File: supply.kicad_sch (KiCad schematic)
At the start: 55 parts, among them Q1 BSS138PW,115, U21 TPS62A06DRLR, U302 AP62301_TSOT, U40 SIC431AED-T1-GE3

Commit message: [#100765] Update schematic
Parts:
- removed C306, C314, C317: C_22u_25V_0805, antmicro-footprints:C_0805_2012Metric, symbol antmicroCapacitorsmisc:C_22u_25V_0805
- removed C309: C_100n_0402, antmicro-footprints:C_0402_1005Metric, symbol antmicroCapacitors0402:C_100n_0402
- removed C88, C89, C90, C91: C_10u_0402, antmicro-footprints:C_0402_1005Metric, symbol antmicroCapacitors0402:C_10u_0402
- removed L3: L_2u2_5.8A_WE-PMFI-35329222, antmicro-footprints:L_WE-PMFI-353220, symbol antmicroFixedInductors:L_2u2_5.8A_WE-PMFI-35329222
- removed R179: R_0R_22.4A_0603, jetson-orin-baseboard-footprints:R_0603_1608Metric, symbol jetson-orin-baseboard:R_0R_22.4A_0603
- removed R18: R_12k4_0402, antmicro-footprints:R_0402_1005Metric, symbol antmicroResistors0402:R_12k4_0402
- removed R19: R_13k7_0402, antmicro-footprints:R_0402_1005Metric, symbol antmicroResistors0402:R_13k7_0402
- removed R20: R_47k_0402, antmicro-footprints:R_0402_1005Metric, symbol antmicroResistors0402:R_47k_0402
- removed R312: R_10k_0402, antmicro-footprints:R_0402_1005Metric, symbol antmicroResistors0402:R_10k_0402
- removed R323: R_0R_22.4A_0603, antmicro-footprints:R_0603_1608Metric, symbol antmicroResistors0603:R_0R_22.4A_0603
- removed TP309: TP_0.75mm_SMD, antmicro-footprints:TP_SMD_0.75mm, symbol antmicroTestPoints:TP_0.75mm_SMD
- removed U302: AP62301_TSOT, antmicro-footprints:TSOT23-6, symbol antmicroDCDCConverters:AP62301_TSOT
- added C60, C61: C_47u_0603, antmicro-footprints:C_0603_1608Metric, symbol antmicroCapacitors0603:C_47u_0603
- added C62, C63: C_22u_0603, antmicro-footprints:C_0603_1608Metric, symbol antmicroCapacitors0603:C_22u_0603
- added C84, C85: C_10u_0402, antmicro-footprints:C_0402_1005Metric, symbol antmicroCapacitors0402:C_10u_0402
- added C86: C_1u_0402, antmicro-footprints:C_0402_1005Metric, symbol antmicroCapacitors0402:C_1u_0402
- added C92: C_120p_100V_0402, antmicro-footprints:C_0402_1005Metric, symbol antmicroCapacitors0402:C_120p_100V_0402
- added D18: LED_G_0603_LG_L29K-G2J1-24-Z, antmicro-footprints:LED_0603_1608Metric_G, symbol antmicroLEDIndicationDiscrete:LED_G_0603_LG_L29K-G2J1-24-Z
- added L4: L_220n_5.9A_1008, antmicro-footprints:L_1008_2520Metric, symbol antmicroFixedInductors:L_220n_5.9A_1008
- added Q6: BSS138PW,115, antmicro-footprints:SC70-3, symbol antmicroTransistorsFETsMOSFETsSingle:BSS138PW,115
- added R148: R_100k_0.1%_0402, antmicro-footprints:R_0402_1005Metric, symbol antmicroResistors0402:R_100k_0402
- added R20: R_470R_0402, antmicro-footprints:R_0402_1005Metric, symbol antmicroResistors0402:R_470R_0402
- added R69, R81: R_0R_22.4A_0603, antmicro-footprints:R_0603_1608Metric, symbol antmicroResistors0603:R_0R_22.4A_0603
- added R77: R_1k5_0402, antmicro-footprints:R_0402_1005Metric, symbol antmicroResistors0402:R_1k5_0402
- added R78: R_10k_0402, antmicro-footprints:R_0402_1005Metric, symbol antmicroResistors0402:R_10k_0402
- added R79: R_33R_0402, antmicro-footprints:R_0402_1005Metric, symbol antmicroResistors0402:R_33R_0402
- added R80: R_200k_0402, antmicro-footprints:R_0402_1005Metric, symbol antmicroResistors0402:R_200k_0402
- added TP30: TP_1mm_SMD, antmicro-footprints:TP_SMD_1mm, symbol antmicroTestPoints:TP_1mm_SMD
- added U22: TPS62A06DRLR, antmicro-footprints:SOT-563, symbol antmicroDCDCConverters:TPS62A06DRLR
- C121, C125: footprint jetson-orin-baseboard-footprints:C_0402_1005Metric -> antmicro-footprints:C_0402_1005Metric; symbol jetson-orin-baseboard:C_100n_0402 -> antmicroCapacitors0402:C_100n_0402
- C122, C151: footprint jetson-orin-baseboard-footprints:C_0805_2012Metric -> antmicro-footprints:C_0805_2012Metric; symbol jetson-orin-baseboard:C_22u_25V_0805 -> antmicroCapacitorsmisc:C_22u_25V_0805
- C123: footprint jetson-orin-baseboard-footprints:C_0402_1005Metric -> antmicro-footprints:C_0402_1005Metric; symbol jetson-orin-baseboard:C_1u_0402 -> antmicroCapacitors0402:C_1u_0402
- C126, C127, C128, C154: footprint jetson-orin-baseboard-footprints:C_0603_1608Metric_EIA -> antmicro-footprints:C_0603_1608Metric_EIA; symbol jetson-orin-baseboard:C_22u_16V_0603 -> antmicroCapacitors0603:C_22u_16V_0603
- C155: footprint jetson-orin-baseboard-footprints:C_0402_1005Metric -> antmicro-footprints:C_0402_1005Metric; symbol jetson-orin-baseboard:C_4u7_25V_0402 -> antmicroCapacitors0402:C_4u7_25V_0402
- D33: footprint jetson-orin-baseboard-footprints:SOD-923 -> antmicro-footprints:SOD-923; symbol jetson-orin-baseboard:ESD9X5.0ST5G -> antmicroTVSDiodes:ESD9X5.0ST5G
- L1: footprint jetson-orin-baseboard-footprints:L_Bourns-SRP5030CA -> antmicro-footprints:L_Bourns-SRP5030CA; symbol jetson-orin-baseboard:L_560n_17.7A_Bourns-SRP5030CA -> antmicroFixedInductors:L_560n_17.7A_Bourns-SRP5030CA
- R147: symbol antmicroResistors0402:R_100k_0.1%_0402 -> antmicroResistors0402:R_100k_0402; MPN RC0402BR-07100KL -> CR0402-FX-1003GLF; Manufacturer YAGEO -> Bourns; Tolerance 0.1% -> 1%
- R173, R176: footprint jetson-orin-baseboard-footprints:R_0402_1005Metric -> antmicro-footprints:R_0402_1005Metric; symbol jetson-orin-baseboard:R_499k_0402 -> antmicroResistors0402:R_499k_0402
- R178: footprint jetson-orin-baseboard-footprints:R_0603_1608Metric -> antmicro-footprints:R_0603_1608Metric; symbol jetson-orin-baseboard:R_0R_22.4A_0603 -> antmicroResistors0603:R_0R_22.4A_0603
- R240: footprint jetson-orin-baseboard-footprints:R_0402_1005Metric -> antmicro-footprints:R_0402_1005Metric; symbol jetson-orin-baseboard:R_499k_0402 -> antmicroResistors0402:R_499k_0402; now in the parts list
- TP54: footprint jetson-orin-baseboard-footprints:TP_SMD_0.75mm -> antmicro-footprints:TP_SMD_0.75mm; symbol jetson-orin-baseboard:TP_0.75mm_SMD -> antmicroTestPoints:TP_0.75mm_SMD
- U40: footprint jetson-orin-baseboard-footprints:MLP44-24L_4x4x0.75mm -> antmicro-footprints:MLP44-24L_4x4x0.75mm; symbol jetson-orin-baseboard:SIC431AED-T1-GE3 -> antmicroDCDCConverters:SIC431AED-T1-GE3
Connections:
- net +0V95: now also R69.2
- net +1V8: now also R81.2, TP30.1
- net +3V3: now also C84.2, C85.2, R20.2, R77.1, R78.2, U22.3 (VIN)
- net DCDC_EN: now also C86.1, R77.2, U22.4 (EN)
- net GND: now also C60.1, C61.1, C62.1, C63.1, C84.1, C85.1, C86.2, Q6.2 (S), R148.1, U22.1 (GND)
- net at C87.2, L2.2, R17.2: now also C60.2, C61.2, R69.1
- new net: D18.2 (A), R20.1
- new net: C62.2, C63.2, C92.2, L4.2, R80.2, R81.1
- new net: C92.1, R148.2, R80.1, U22.5 (FB)
- new net: Q6.1 (G), R78.1, R79.1
- new net: D18.1 (C), Q6.3 (D)
- new net: R79.2, U22.6 (PG)
- new net: L4.1, U22.2 (SW)
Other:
- note added: "JOB VCC to 3V3 DCDC Converter"
- note added: "PG: OD in Power Good state"
- note added: "V_{OUT} = 0.6*(200k/100k + 1)"
- note added: "V_{OUT} = 1.8V"
- note removed: "3V3 DCDC"
- moved on the sheet: C81, C82, C83, C87, D17, L2, Q1, R147, R15, R16, R17, R66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

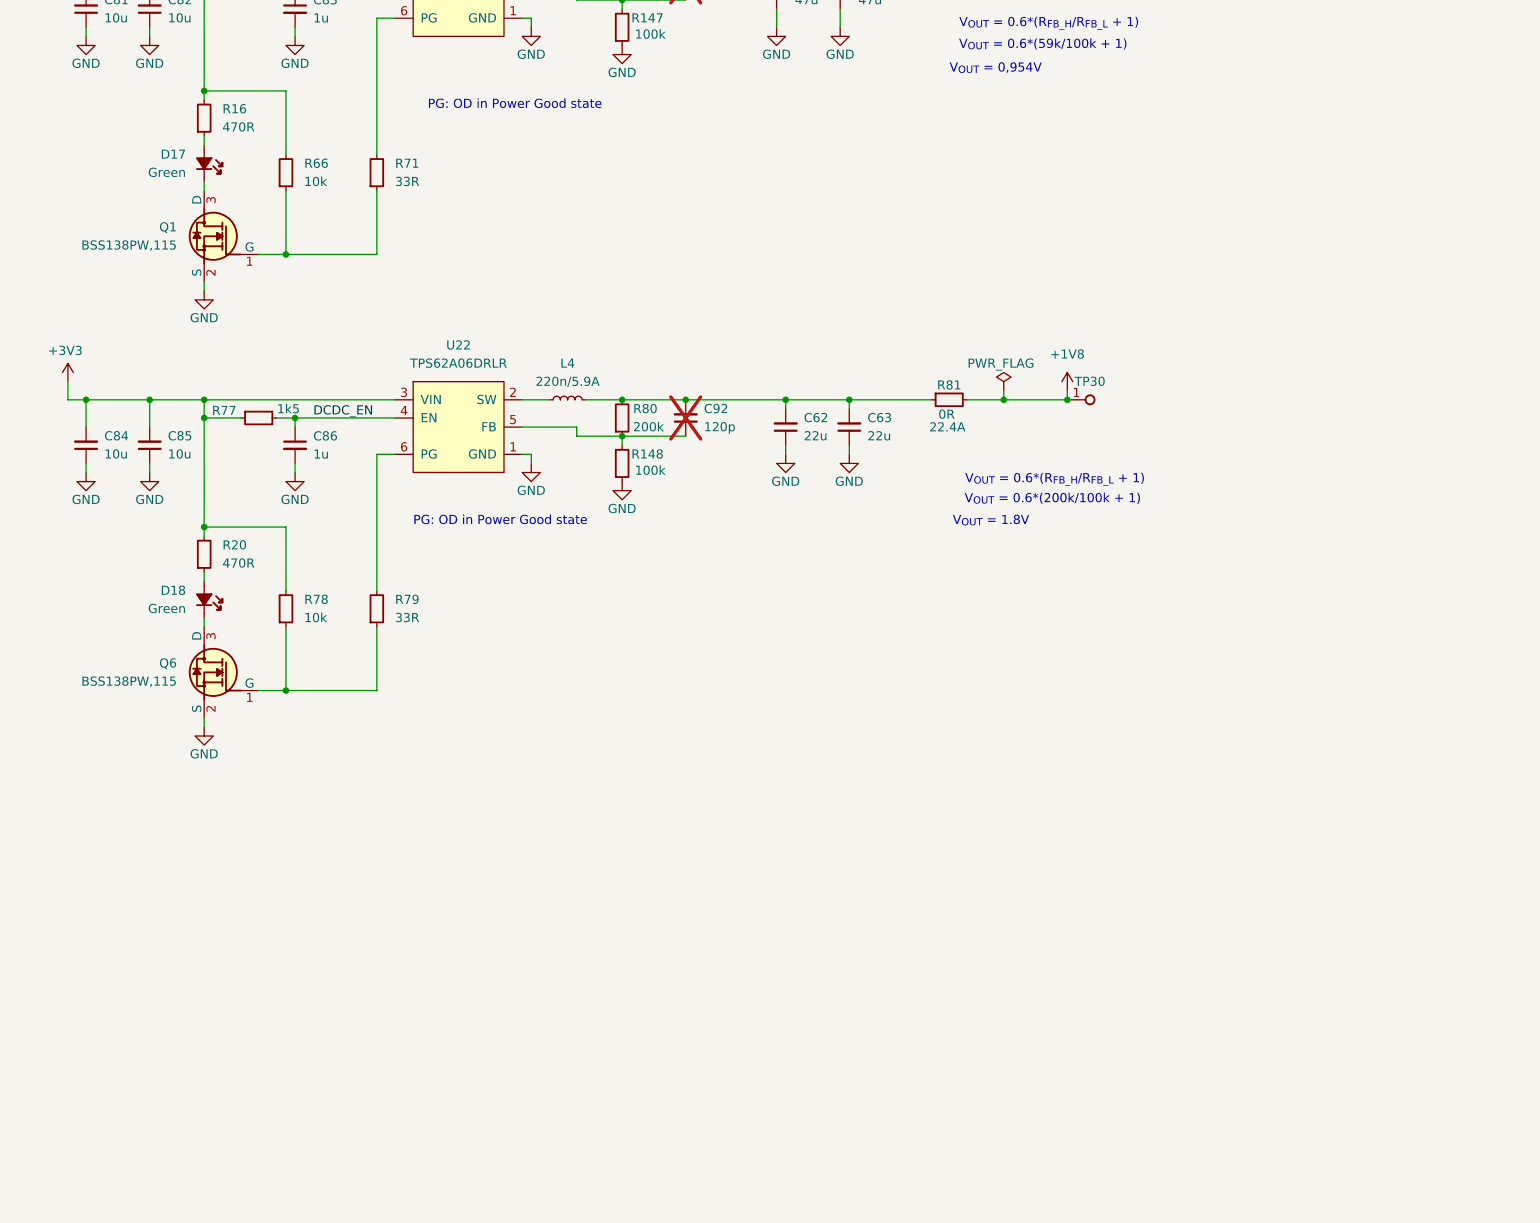
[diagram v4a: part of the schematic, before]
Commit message: [#100765] Change sheet format to A3, update schematic
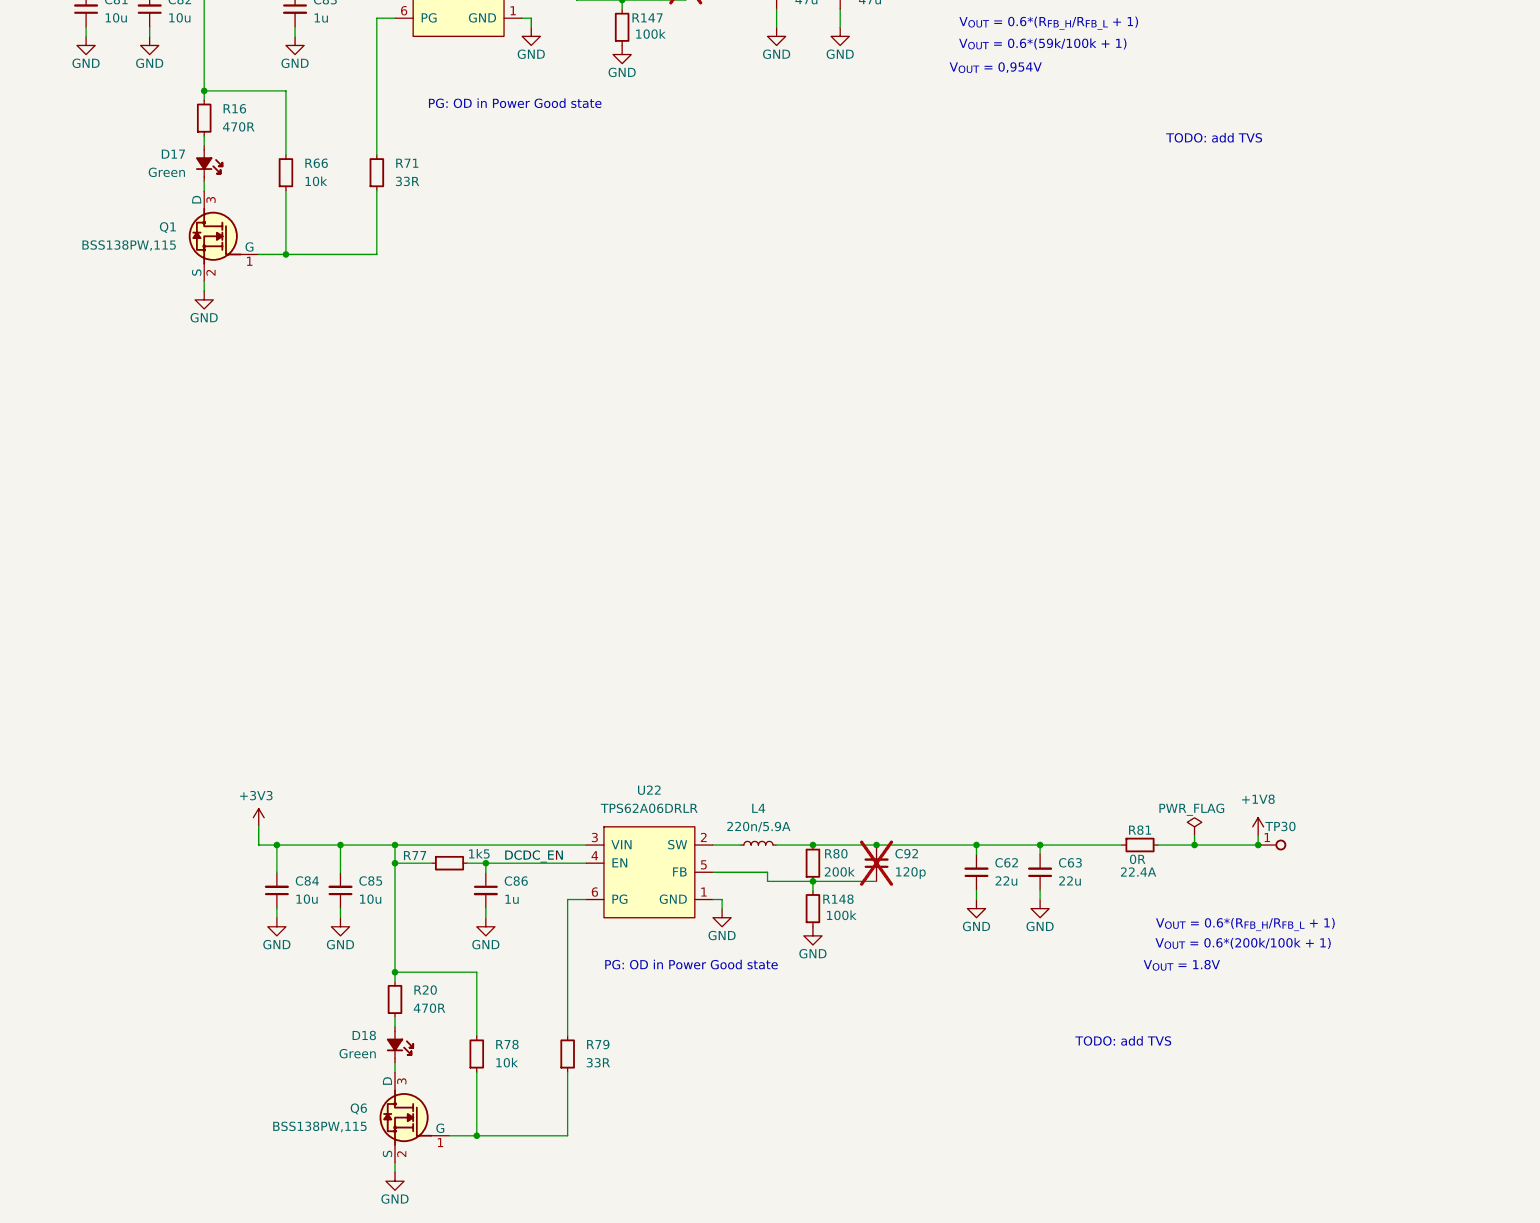
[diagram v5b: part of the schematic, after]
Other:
- note added: "TODO: add TVS"
- company: (none) -> Antmicro
- title: (none) -> antmicro-jetson-orin-baseboard-pcie-switch-expansion-hw
- moved on the sheet: C62, C63, C84, C85, C86, C92, D18, L4, Q6, R148, R20, R77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

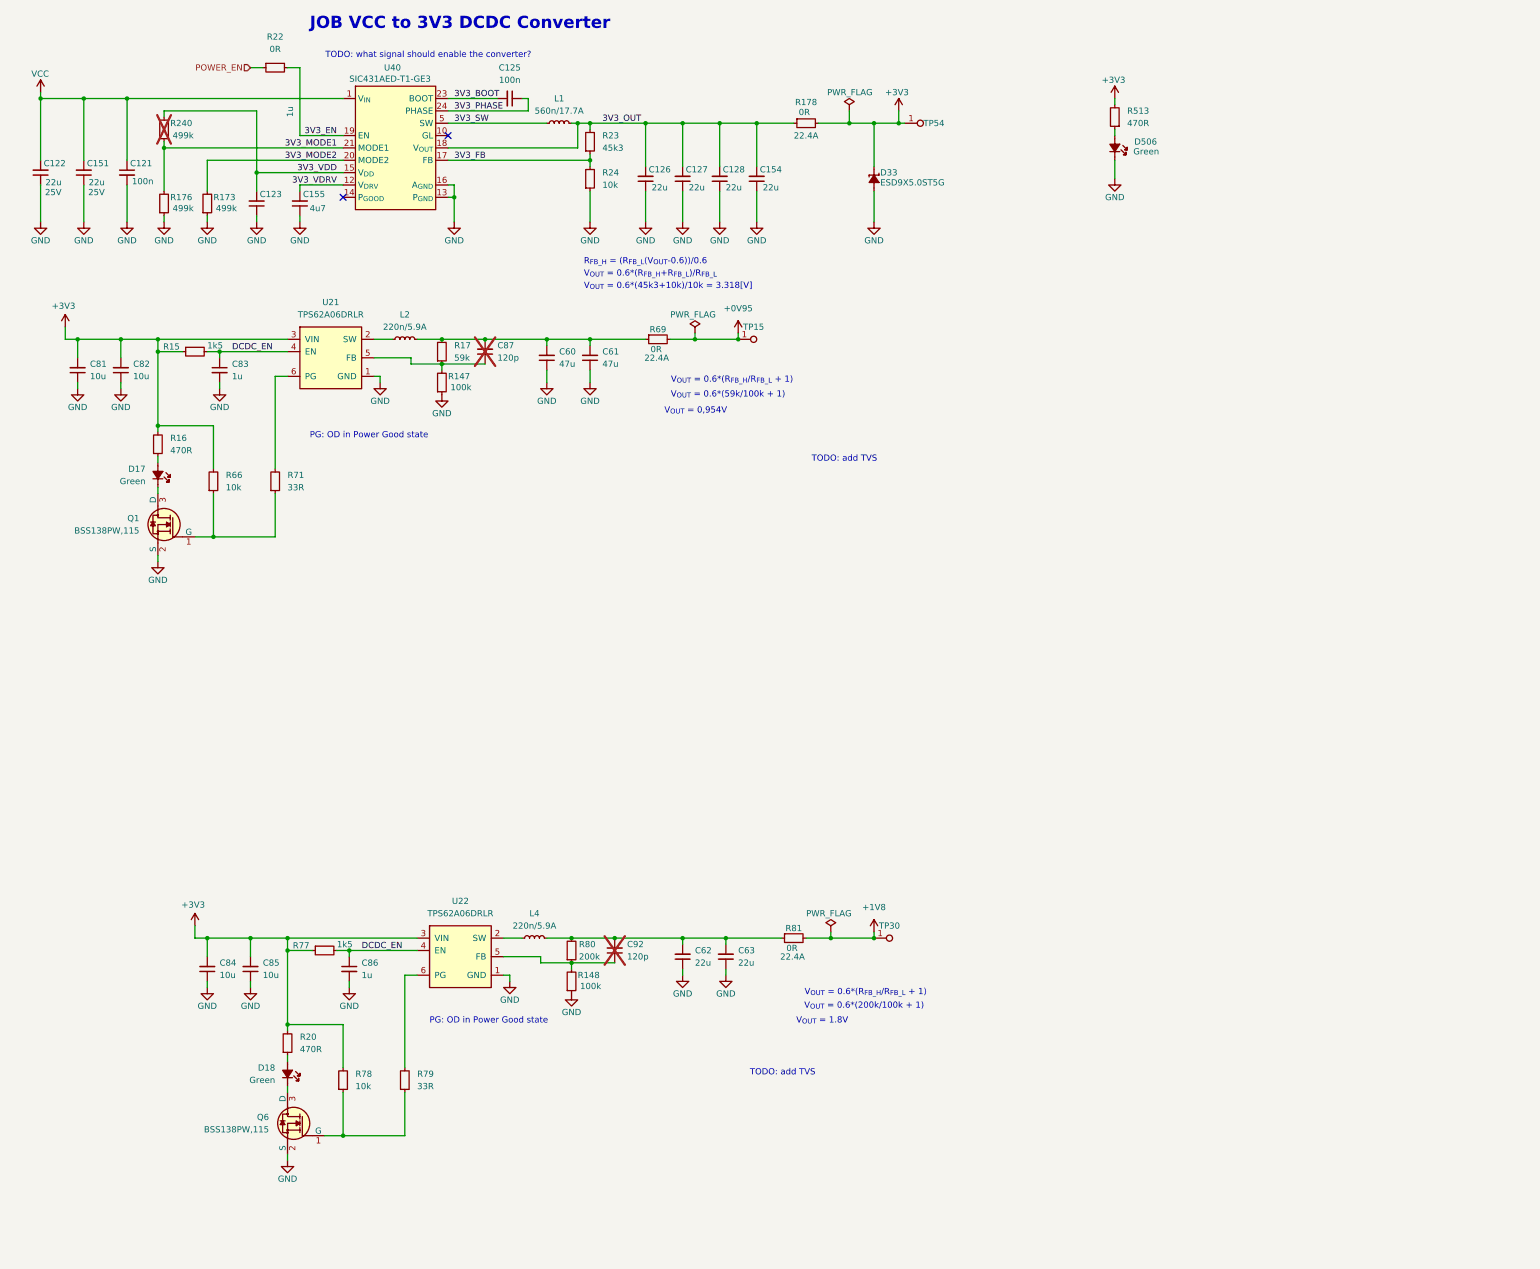
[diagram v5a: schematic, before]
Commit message: [#100765] Prettify decoupling caps
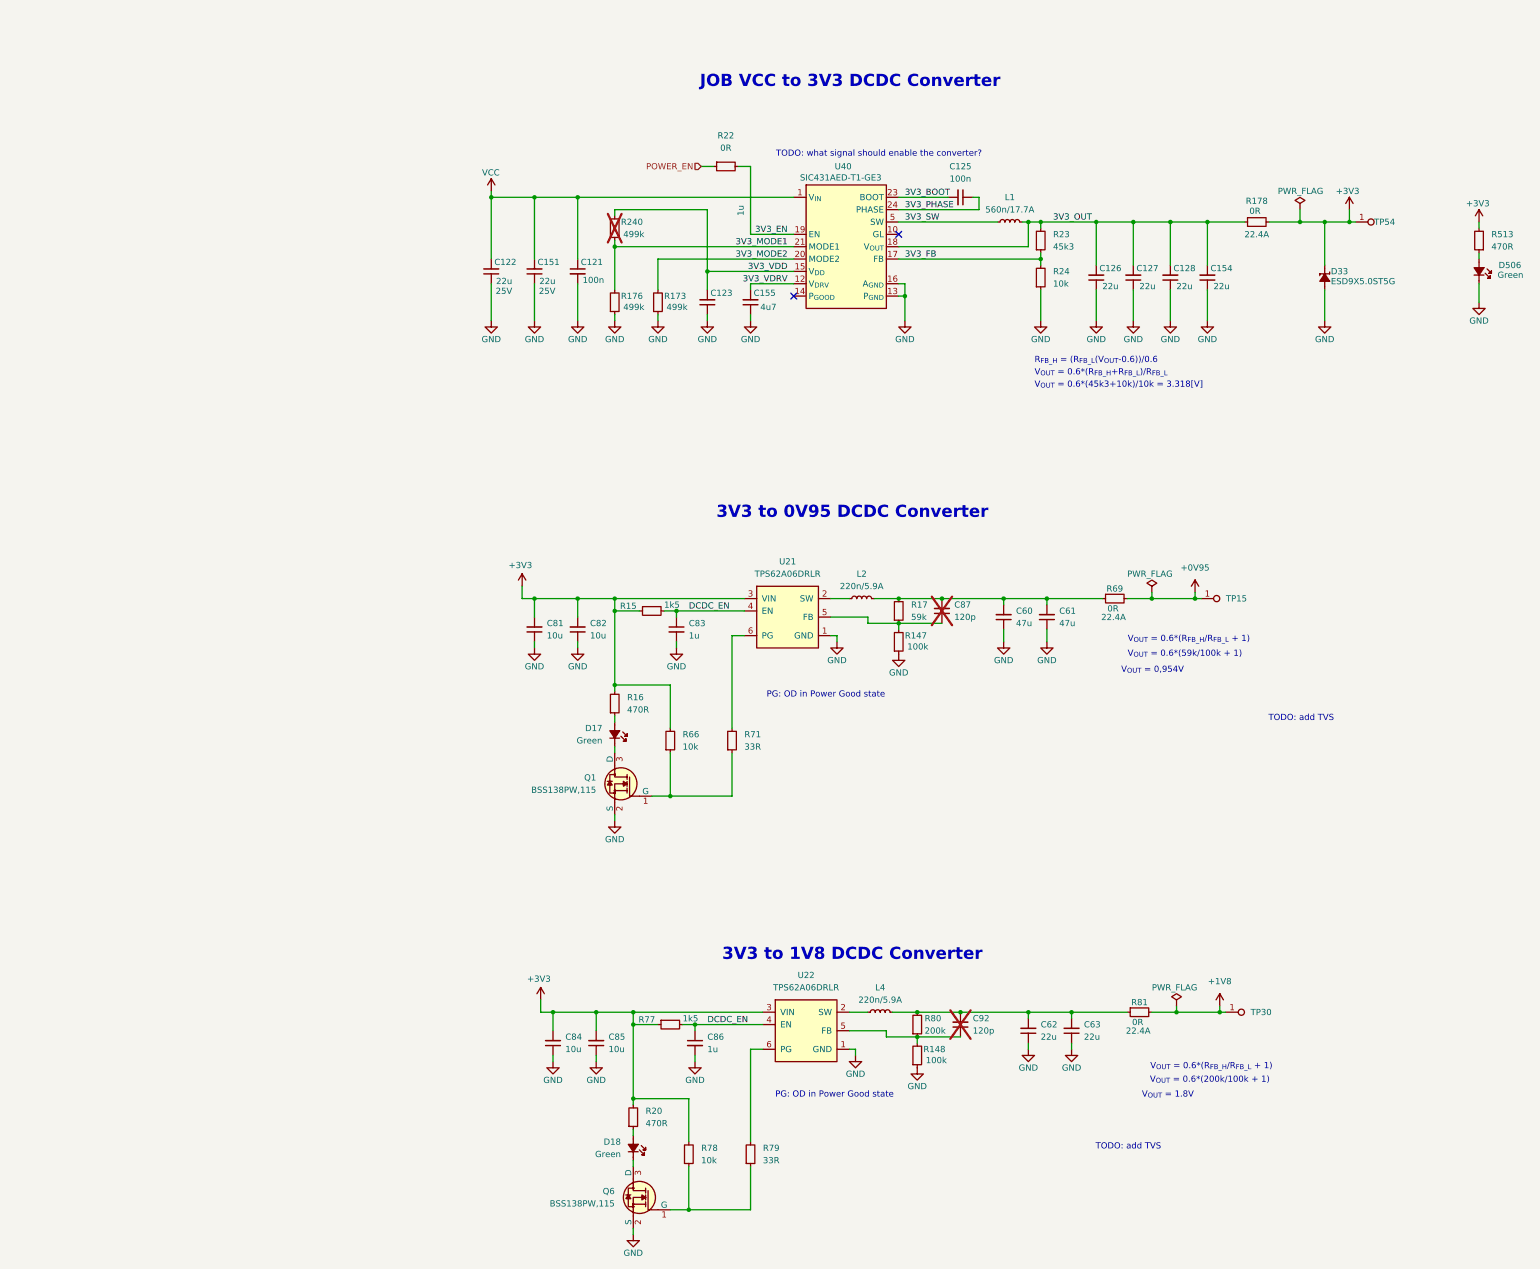
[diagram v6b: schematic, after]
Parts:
- removed TP15, TP30: TP_1mm_SMD, antmicro-footprints:TP_SMD_1mm, symbol antmicroTestPoints:TP_1mm_SMD
- added TP15, TP30: TP_0.75mm_SMD, antmicro-footprints:TP_SMD_0.75mm, symbol antmicroTestPoints:TP_0.75mm_SMD
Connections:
- net +0V95: now also TP15.1
- net +1V8: now also TP30.1
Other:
- note added: "3V3 to 0V95 DCDC Converter"
- note added: "3V3 to 1V8 DCDC Converter"
- moved on the sheet: C121, C122, C123, C125, C126, C127, C128, C151, C154, C155, C60, C61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

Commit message: [#100765] WIP: Apply review changes
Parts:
- added R110: R_10k_0402, antmicro-footprints:R_0402_1005Metric, symbol antmicroResistors0402:R_10k_0402
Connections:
- net 3V3_EN: now also R110.2
- net VCC: now also R110.1
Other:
- note removed: "TODO: what signal should enable the converter?"
